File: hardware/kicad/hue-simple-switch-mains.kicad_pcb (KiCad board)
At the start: 2 copper layers, 42 x 52 mm, 28 parts, among them J1 MAINS L/N, J2 D0 D1 D2 D3, J3 D4 D5 GND, U1 XIAO ESP32-C6

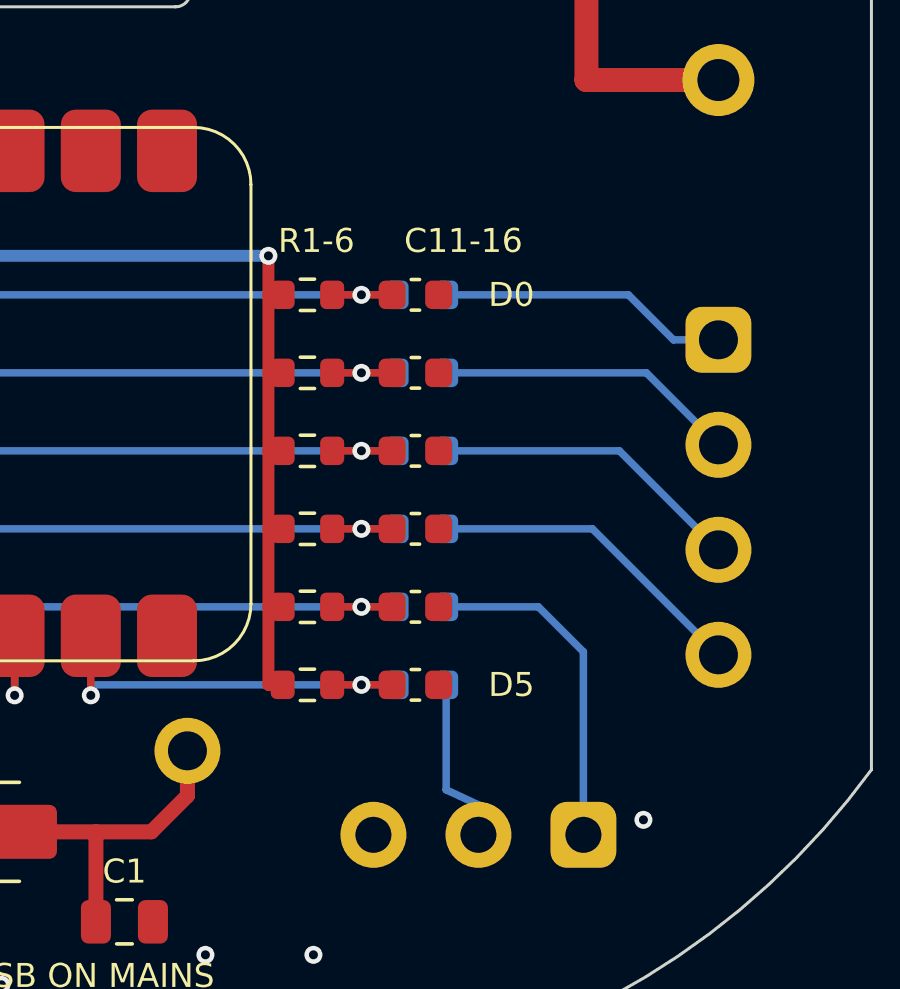
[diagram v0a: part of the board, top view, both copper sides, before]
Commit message: 3-board JLCPCB assembly panel, one-sided SMD, centred CPL (#30)
* Add a 3-board JLCPCB assembly panel, one-sided SMD, centred CPL

- R11-R16 move to the XIAO side, so every SMD part is on one side (no
  second stencil or double-sided assembly). Each input row is now
  pull-up, 1k, 10nF; the 10nF sits at the terminal side of the 1k.
- build_panel.py: three boards on a 144 x 71 mm frame (over JLCPCB's
  70 x 70 minimum, so no extra rails), routed tabs with mouse bites,
  three fiducials, four tooling holes. Order 5 panels = 15 boards.
  Panel DRC runs in build_all; mouse bites keep >= 1 mm from mains.
- CPL written from the board: each part at its pad centre, not the
  footprint origin (KiCad puts through-hole origins on pin 1, which put
  PS1 15 mm and J2 5 mm off in JLCPCB's preview). Panel BOM/CPL use
  per-board designators (R1_1 ...) and leave out the XIAO.
- README: ordering on the panel, and which parts to check in the
  preview (D1, PS1, J1-J3).

Co-Authored-By: Claude Opus 5.5 <noreply@anthropic.com>

* Panel: side tabs between the boards and to the frame

Each board was held only by four tabs on its round ends. Add a tab on
each straight side at y = -3 mm (between J1 and J2 on the right, clear of
the XIAO pads on the left), tying neighbours together and the outer boards
to the side frame, so the row stays stiff while the through-hole parts are
inserted and soldered. Mouse bites on every board edge; panel DRC clean.

Co-Authored-By: Claude Opus 5.5 <noreply@anthropic.com>

---------

Co-authored-by: Claude Opus 5.5 <noreply@anthropic.com>
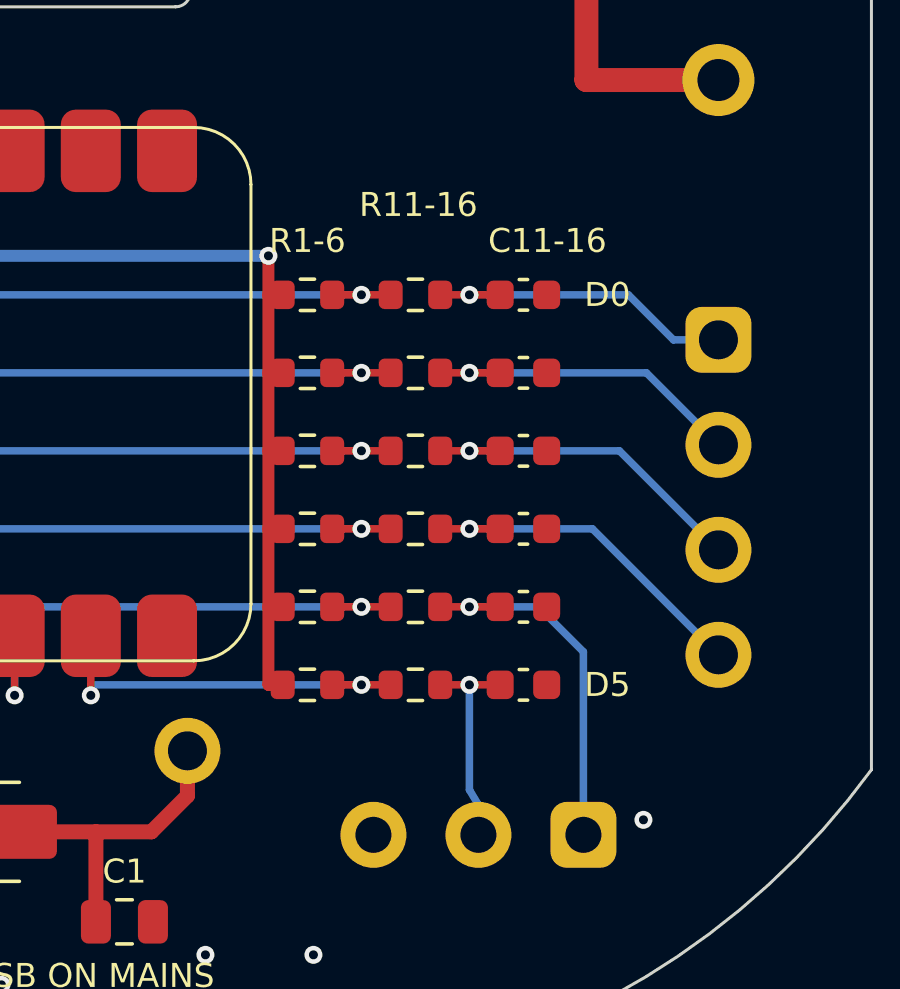
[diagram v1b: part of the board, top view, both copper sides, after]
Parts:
- R11, R12, R13, R14, R15, R16: moved to F.Cu
- moved C11 3.60 mm to (109.4, 99.5)
- moved C12 3.60 mm to (109.4, 102.1)
- moved C13 3.60 mm to (109.4, 104.7)
- moved C14 3.60 mm to (109.4, 107.3)
- moved C15 3.60 mm to (109.4, 109.9)
- moved C16 3.60 mm to (109.4, 112.5)
- moved R11 0.20 mm to (105.8, 99.5)
- moved R12 0.20 mm to (105.8, 102.1)
- moved R13 0.20 mm to (105.8, 104.7)
- moved R14 0.20 mm to (105.8, 107.3)
- moved R15 0.20 mm to (105.8, 109.9)
- moved R16 0.20 mm to (105.8, 112.5)
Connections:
- C11 pad 1: D0 -> IN_D0
- C12 pad 1: D1 -> IN_D1
- C13 pad 1: D2 -> IN_D2
- C14 pad 1: D3 -> IN_D3
- C15 pad 1: D4 -> IN_D4
- C16 pad 1: D5 -> IN_D5
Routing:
- net IN_D5: track 5.69 -> 7.08 mm, vias 0 -> 1
- net IN_D4: track 11.3 -> 12.5 mm, vias 0 -> 1
- net IN_D3: track 10.8 -> 12.0 mm, vias 0 -> 1
- net IN_D2: track 10.4 -> 11.7 mm, vias 0 -> 1
- net IN_D1: track 10.1 -> 11.3 mm, vias 0 -> 1
- net IN_D0: track 9.70 -> 10.9 mm, vias 0 -> 1
- net D5: track 14.5 -> 13.3 mm
- net D4: track 19.7 -> 18.4 mm
- net D3: track 24.8 -> 23.6 mm
- net D2: track 29.9 -> 28.7 mm
- net D1: track 35.1 -> 33.9 mm
- net D0: track 40.2 -> 39.0 mm
